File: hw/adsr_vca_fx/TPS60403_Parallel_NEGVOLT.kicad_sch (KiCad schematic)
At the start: 9 parts

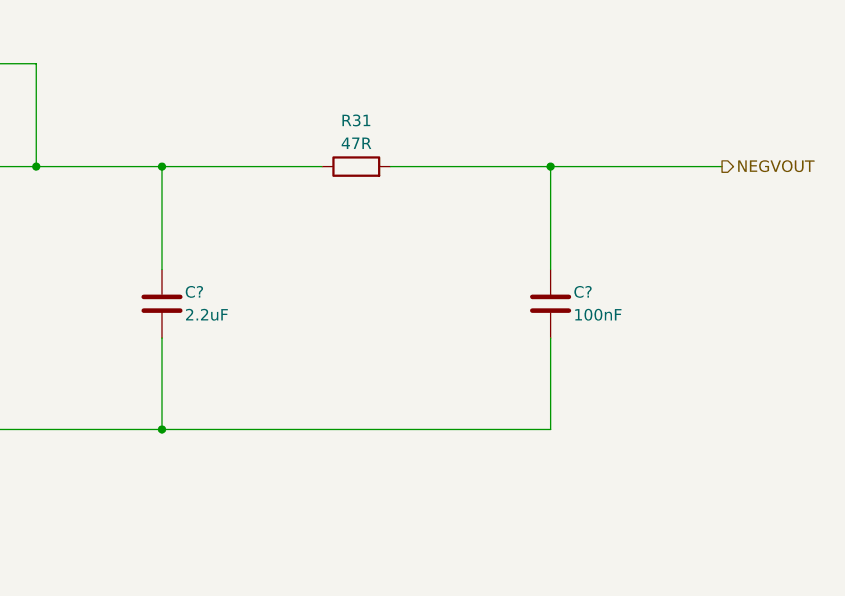
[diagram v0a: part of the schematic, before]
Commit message: renamed sheet
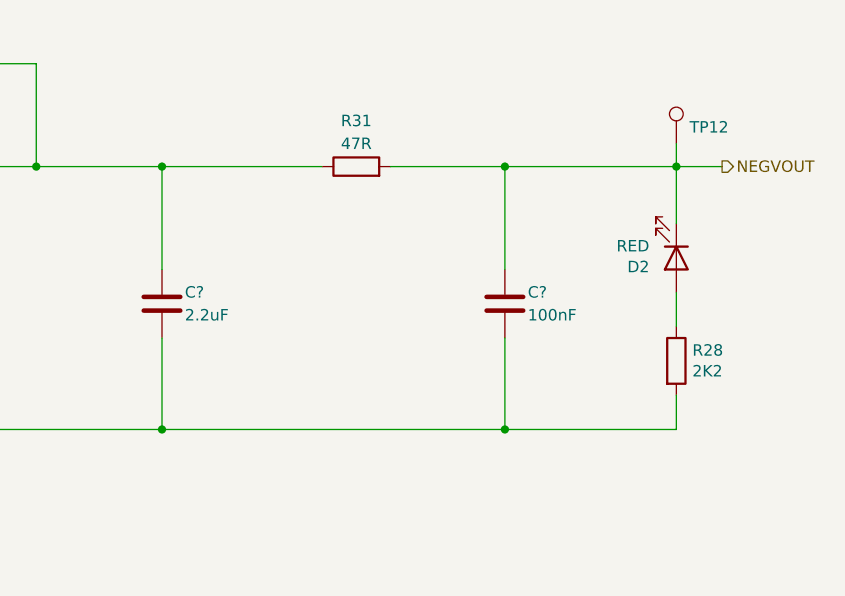
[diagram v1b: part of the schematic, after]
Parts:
- added D2: RED, LED_SMD:LED_0805_2012Metric_Pad1.15x1.40mm_HandSolder, symbol Device:LED
- added R28: 2K2, Resistor_SMD:R_0805_2012Metric_Pad1.20x1.40mm_HandSolder, symbol Device:R
- added TP12: TestPoint, TestPoint:TestPoint_Pad_D1.0mm, symbol Connector:TestPoint
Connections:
- net GND: now also R28.2
- net NEGVOUT: now also D2.1 (K), TP12.1
- new net: D2.2 (A), R28.1
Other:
- moved on the sheet: C?
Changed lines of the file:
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@@
 (kicad_sch (version 20230121) (generator eeschema)
   (paper "A4")
-  (junction (at 240.03 69.85) (diameter 0) (color 0 0 0 0)
-  )
   (junction (at 196.85 99.06) (diameter 0) (color 0 0 0 0)
   )
@@
   (junction (at 66.04 55.88) (diameter 0) (color 0 0 0 0)
   )
+  (junction (at 234.95 99.06) (diameter 0) (color 0 0 0 0)
+  )
   (junction (at 182.88 69.85) (diameter 0) (color 0 0 0 0)
   )
   (junction (at 176.53 99.06) (diameter 0) (color 0 0 0 0)
   )
+  (junction (at 254 69.85) (diameter 0) (color 0 0 0 0)
+  )
+  (junction (at 234.95 69.85) (diameter 0) (color 0 0 0 0)
+  )
   (wire (pts (xy 196.85 69.85) (xy 196.85 81.28))
     (stroke (width 0) (type default))
@@
     (stroke (width 0) (type default))
   )
+  (wire (pts (xy 254 69.85) (xy 254 67.31))
+    (stroke (width 0) (type default))
+  )
   (wire (pts (xy 87.63 72.39) (xy 93.98 72.39))
     (stroke (width 0) (type default))
   )
-  (wire (pts (xy 240.03 69.85) (xy 240.03 81.28))
+  (wire (pts (xy 234.95 69.85) (xy 234.95 81.28))
     (stroke (width 0) (type default))
   )
@@
     (stroke (width 0) (type default))
   )
+  (wire (pts (xy 234.95 99.06) (xy 254 99.06))
+    (stroke (width 0) (type default))
+  )
+  (wire (pts (xy 254 87.63) (xy 254 83.82))
+    (stroke (width 0) (type default))
+  )
   (wire (pts (xy 123.19 82.55) (xy 123.19 99.06))
     (stroke (width 0) (type default))
@@
     (stroke (width 0) (type default))
   )
-  (wire (pts (xy 240.03 99.06) (xy 196.85 99.06))
+  (wire (pts (xy 254 69.85) (xy 254 76.2))
     (stroke (width 0) (type default))
   )
@@
     (stroke (width 0) (type default))
   )
-  (wire (pts (xy 240.03 88.9) (xy 240.03 99.06))
+  (wire (pts (xy 234.95 88.9) (xy 234.95 99.06))
     (stroke (width 0) (type default))
   )
@@
     (stroke (width 0) (type default))
   )
-  (wire (pts (xy 222.25 69.85) (xy 240.03 69.85))
-    (stroke (width 0) (type default))
-  )
-  (wire (pts (xy 240.03 69.85) (xy 259.08 69.85))
+  (wire (pts (xy 222.25 69.85) (xy 234.95 69.85))
+    (stroke (width 0) (type default))
+  )
+  (wire (pts (xy 234.95 99.06) (xy 196.85 99.06))
+    (stroke (width 0) (type default))
+  )
+  (wire (pts (xy 254 69.85) (xy 259.08 69.85))
+    (stroke (width 0) (type default))
+  )
+  (wire (pts (xy 254 95.25) (xy 254 99.06))
+    (stroke (width 0) (type default))
+  )
+  (wire (pts (xy 234.95 69.85) (xy 254 69.85))
     (stroke (width 0) (type default))
   )
@@
     )
   )
+  (symbol (lib_id "Device:R") (at 254 91.44 0) (unit 1)
+    (in_bom yes) (on_board yes) (dnp no)
+    (property "Reference" "R28" (at 255.778 90.2716 0)
+      (effects (font (size 1.27 1.27)) (justify left))
+    )
+    (property "Value" "2K2" (at 255.778 92.583 0)
+      (effects (font (size 1.27 1.27)) (justify left))
+    )
+    (property "Footprint" "Resistor_SMD:R_0805_2012Metric_Pad1.20x1.40mm_HandSolder" (at 252.222 91.44 90)
+      (effects (font (size 1.27 1.27)) hide)
+    )
+    (property "Datasheet" "~" (at 254 91.44 0)
+      (effects (font (size 1.27 1.27)) hide)
+    )
+    (property "LcscNo" "~" (at 254 91.44 0)
+      (effects (font (size 1.27 1.27)) hide)
+    )
+    (property "Type" "~" (at 254 91.44 0)
+      (effects (font (size 1.27 1.27)) hide)
+    )
+    (pin "1")
+    (pin "2")
+    (instances
+      (project "adsr_vca_fx"
+        (path "/2c7cc946-dcca-4ffb-b6a0-bf0c9ddb491b/d2509004-b5c4-4b3c-af62-d7c90bd19790/2b12c81b-590f-42b3-a93e-f9019ce43b66"
+          (reference "R28") (unit 1)
+        )
+        (path "/2c7cc946-dcca-4ffb-b6a0-bf0c9ddb491b/d2509004-b5c4-4b3c-af62-d7c90bd19790/8209921e-d4bf-4a54-a276-7037229ad038"
+          (reference "R20") (unit 1)
+        )
+      )
+    )
+  )
   (symbol (lib_id "TPS6040x:TPS60400") (at 104.14 76.2 0) (unit 1)
     (in_bom yes) (on_board yes) (dnp no) (fields_autoplaced)
@@
     )
   )
-  (symbol (lib_id "Device:C") (at 240.03 85.09 0) (unit 1)
+  (symbol (lib_id "Device:C") (at 234.95 85.09 0) (unit 1)
     (in_bom yes) (on_board yes) (dnp no)
-    (property "Reference" "C?" (at 242.57 83.82 0)
-      (effects (font (size 1.27 1.27)) (justify left))
-    )
-    (property "Value" "100nF" (at 242.57 86.36 0)
-      (effects (font (size 1.27 1.27)) (justify left))
-    )
-    (property "Footprint" "Capacitor_SMD:C_0805_2012Metric_Pad1.18x1.45mm_HandSolder" (at 240.9952 88.9 0)
-      (effects (font (size 1.27 1.27)) hide)
-    )
-    (property "Datasheet" "~" (at 240.03 85.09 0)
+    (property "Reference" "C?" (at 237.49 83.82 0)
+      (effects (font (size 1.27 1.27)) (justify left))
+    )
+    (property "Value" "100nF" (at 237.49 86.36 0)
+      (effects (font (size 1.27 1.27)) (justify left))
+    )
+    (property "Footprint" "Capacitor_SMD:C_0805_2012Metric_Pad1.18x1.45mm_HandSolder" (at 235.9152 88.9 0)
+      (effects (font (size 1.27 1.27)) hide)
+    )
+    (property "Datasheet" "~" (at 234.95 85.09 0)
       (effects (font (size 1.27 1.27)) hide)
     )
@@
     )
   )
+  (symbol (lib_id "Device:LED") (at 254 80.01 270) (unit 1)
+    (in_bom yes) (on_board yes) (dnp no)
+    (property "Reference" "D2" (at 251.0028 81.0006 90)
+      (effects (font (size 1.27 1.27)) (justify right))
+    )
+    (property "Value" "RED" (at 251.0028 78.6892 90)
+      (effects (font (size 1.27 1.27)) (justify right))
+    )
+    (property "Footprint" "LED_SMD:LED_0805_2012Metric_Pad1.15x1.40mm_HandSolder" (at 254 80.01 0)
+      (effects (font (size 1.27 1.27)) hide)
+    )
+    (property "Datasheet" "~" (at 254 80.01 0)
+      (effects (font (size 1.27 1.27)) hide)
+    )
+    (property "LcscNo" "C2293" (at 254 80.01 0)
+      (effects (font (size 1.27 1.27)) hide)
+    )
+    (property "Type" "~" (at 254 80.01 0)
+      (effects (font (size 1.27 1.27)) hide)
+    )
+    (pin "1")
+    (pin "2")
+    (instances
+      (project "adsr_vca_fx"
+        (path "/2c7cc946-dcca-4ffb-b6a0-bf0c9ddb491b/d2509004-b5c4-4b3c-af62-d7c90bd19790/2b12c81b-590f-42b3-a93e-f9019ce43b66"
+          (reference "D2") (unit 1)
+        )
+        (path "/2c7cc946-dcca-4ffb-b6a0-bf0c9ddb491b/d2509004-b5c4-4b3c-af62-d7c90bd19790/8209921e-d4bf-4a54-a276-7037229ad038"
+          (reference "D5") (unit 1)
+        )
+      )
+    )
+  )
   (symbol (lib_id "Device:C") (at 66.04 83.82 0) (unit 1)
     (in_bom yes) (on_board yes) (dnp no) (fields_autoplaced)
@@
         )
       )
+    )
+  )
+  (symbol (lib_id "Connector:TestPoint") (at 254 67.31 0) (unit 1)
+    (in_bom yes) (on_board yes) (dnp no)
+    (property "Reference" "TP12" (at 255.4732 65.4812 0)
+      (effects (font (size 1.27 1.27)) (justify left))
+    )
+    (property "Value" "TestPoint" (at 255.4732 66.6242 0)
+      (effects (font (size 1.27 1.27)) (justify left) hide)
+    )
+    (property "Footprint" "TestPoint:TestPoint_Pad_D1.0mm" (at 259.08 67.31 0)
+      (effects (font (size 1.27 1.27)) hide)
+    )
+    (property "Datasheet" "~" (at 259.08 67.31 0)
+      (effects (font (size 1.27 1.27)) hide)
+    )
+    (property "LcscNo" "~" (at 254 67.31 0)
+      (effects (font (size 1.27 1.27)) hide)
+    )
+    (property "Type" "~" (at 254 67.31 0)
+      (effects (font (size 1.27 1.27)) hide)
+    )
+    (pin "1")
+    (instances
+      (project "adsr_vca_fx"
+        (path "/2c7cc946-dcca-4ffb-b6a0-bf0c9ddb491b/d2509004-b5c4-4b3c-af62-d7c90bd19790/2b12c81b-590f-42b3-a93e-f9019ce43b66"
+          (reference "TP12") (unit 1)
+        )
+        (path "/2c7cc946-dcca-4ffb-b6a0-bf0c9ddb491b/d2509004-b5c4-4b3c-af62-d7c90bd19790/8209921e-d4bf-4a54-a276-7037229ad038"
+          (reference "TP3") (unit 1)
+        )
+      )

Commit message: first draft layout
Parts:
- renumbered R31 to R27
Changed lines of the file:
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@@
   (symbol (lib_id "Device:R") (at 218.44 69.85 90) (unit 1)
     (in_bom yes) (on_board yes) (dnp no) (fields_autoplaced)
-    (property "Reference" "R31" (at 218.44 64.77 90)
+    (property "Reference" "R27" (at 218.44 64.77 90)
       (effects (font (size 1.27 1.27)))
     )
@@
       (project "adsr_vca_fx"
         (path "/2c7cc946-dcca-4ffb-b6a0-bf0c9ddb491b/d2509004-b5c4-4b3c-af62-d7c90bd19790/8209921e-d4bf-4a54-a276-7037229ad038"
-          (reference "R31") (unit 1)
+          (reference "R27") (unit 1)
         )
       )
@@
   (symbol (lib_id "power:GND") (at 123.19 109.22 0) (unit 1)
     (in_bom yes) (on_board yes) (dnp no) (fields_autoplaced)
-    (property "Reference" "#PWR071" (at 123.19 115.57 0)
+    (property "Reference" "#PWR069" (at 123.19 115.57 0)
       (effects (font (size 1.27 1.27)) hide)
     )
@@
       (project "adsr_vca_fx"
         (path "/2c7cc946-dcca-4ffb-b6a0-bf0c9ddb491b/d2509004-b5c4-4b3c-af62-d7c90bd19790/8209921e-d4bf-4a54-a276-7037229ad038"
-          (reference "#PWR071") (unit 1)
+          (reference "#PWR069") (unit 1)
         )
       )
@@
         )
         (path "/2c7cc946-dcca-4ffb-b6a0-bf0c9ddb491b/d2509004-b5c4-4b3c-af62-d7c90bd19790/8209921e-d4bf-4a54-a276-7037229ad038"
-          (reference "U12") (unit 1)
+          (reference "U9") (unit 1)
         )
       )
@@
         )
         (path "/2c7cc946-dcca-4ffb-b6a0-bf0c9ddb491b/d2509004-b5c4-4b3c-af62-d7c90bd19790/8209921e-d4bf-4a54-a276-7037229ad038"
-          (reference "R20") (unit 1)
+          (reference "R28") (unit 1)
         )
       )
@@
         )
         (path "/2c7cc946-dcca-4ffb-b6a0-bf0c9ddb491b/d2509004-b5c4-4b3c-af62-d7c90bd19790/8209921e-d4bf-4a54-a276-7037229ad038"
-          (reference "U11") (unit 1)
+          (reference "U8") (unit 1)
         )
       )
@@
         )
         (path "/2c7cc946-dcca-4ffb-b6a0-bf0c9ddb491b/d2509004-b5c4-4b3c-af62-d7c90bd19790/8209921e-d4bf-4a54-a276-7037229ad038"
-          (reference "C33") (unit 1)
+          (reference "C27") (unit 1)
         )
       )
@@
         )
         (path "/2c7cc946-dcca-4ffb-b6a0-bf0c9ddb491b/d2509004-b5c4-4b3c-af62-d7c90bd19790/8209921e-d4bf-4a54-a276-7037229ad038"
-          (reference "C30") (unit 1)
+          (reference "C24") (unit 1)
         )
       )
@@
         )
         (path "/2c7cc946-dcca-4ffb-b6a0-bf0c9ddb491b/d2509004-b5c4-4b3c-af62-d7c90bd19790/8209921e-d4bf-4a54-a276-7037229ad038"
-          (reference "C29") (unit 1)
+          (reference "C23") (unit 1)
         )
       )
@@
         )
         (path "/2c7cc946-dcca-4ffb-b6a0-bf0c9ddb491b/d2509004-b5c4-4b3c-af62-d7c90bd19790/8209921e-d4bf-4a54-a276-7037229ad038"
-          (reference "TP3") (unit 1)
+          (reference "TP11") (unit 1)
         )
       )
@@
         )
         (path "/2c7cc946-dcca-4ffb-b6a0-bf0c9ddb491b/d2509004-b5c4-4b3c-af62-d7c90bd19790/8209921e-d4bf-4a54-a276-7037229ad038"
-          (reference "C32") (unit 1)
+          (reference "C26") (unit 1)
         )
       )
@@
         )
         (path "/2c7cc946-dcca-4ffb-b6a0-bf0c9ddb491b/d2509004-b5c4-4b3c-af62-d7c90bd19790/8209921e-d4bf-4a54-a276-7037229ad038"
-          (reference "C31") (unit 1)
-        )
-      )
+          (reference "C25") (unit 1)
+        )
+      )

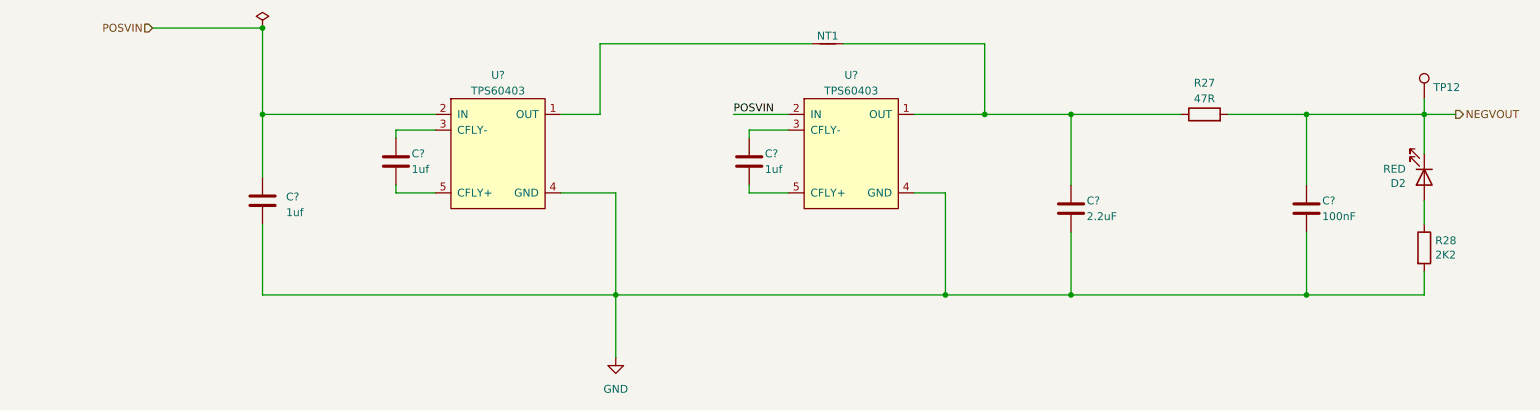
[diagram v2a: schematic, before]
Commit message: updated layout
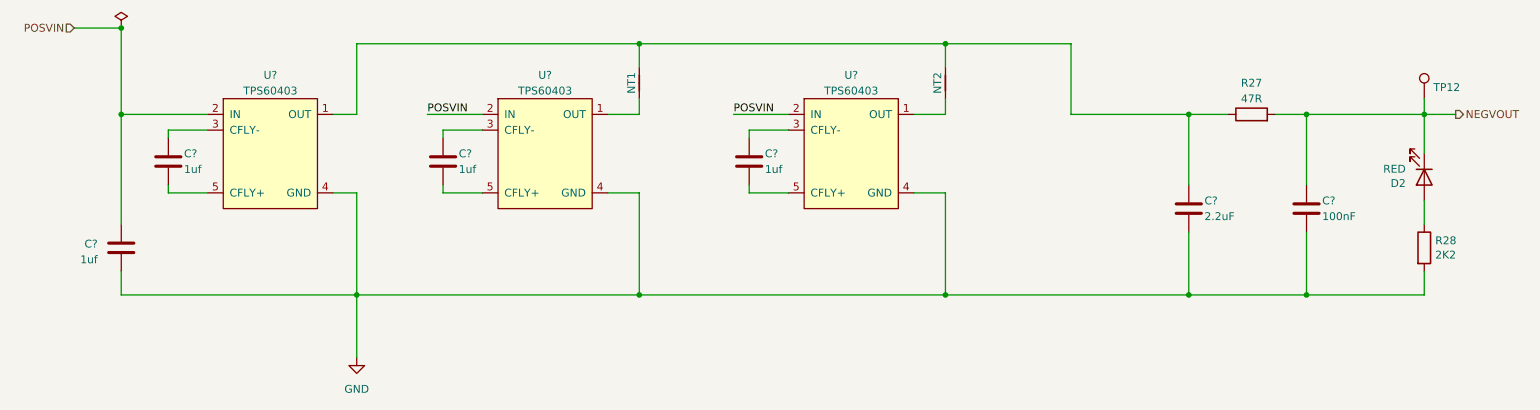
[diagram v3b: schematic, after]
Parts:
- added C?: 1uf, Capacitor_SMD:C_0805_2012Metric_Pad1.18x1.45mm_HandSolder, symbol Device:C
- added NT2: NetTie_2, NetTie:NetTie-2_SMD_Pad0.5mm, symbol Device:NetTie_2
- added U?: TPS60403, Package_TO_SOT_SMD:SOT-23-5_HandSoldering, symbol TPS6040x:TPS60400
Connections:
- net GND: now also U?.4 (GND)
- net POSVIN: now also U?.2 (IN)
- net at C?.1, NT1.2, R27.1: now also U?.1 (OUT), NT2.2; no longer U?.1 (OUT)
- net at NT1.1: now also U?.1 (OUT); no longer U?.1 (OUT)
- new net: NT2.1, U?.1 (OUT)
- new net: C?.1, U?.3 (CFLY-)
- new net: C?.2, U?.5 (CFLY+)
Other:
- moved on the sheet: C?, NT1, R27, U?

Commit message: completed layout
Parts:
- removed TP12: TestPoint, TestPoint:TestPoint_Pad_D1.0mm, symbol Connector:TestPoint
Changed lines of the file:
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@@
-    (stroke (width 0) (type default))
-  )
-  (wire (pts (xy 254 69.85) (xy 254 67.31))
     (stroke (width 0) (type default))
   )
@@
         )
       )
-    )
-  )
-  (symbol (lib_id "Connector:TestPoint") (at 254 67.31 0) (unit 1)
-    (in_bom yes) (on_board yes) (dnp no)
-    (property "Reference" "TP12" (at 255.4732 65.4812 0)
-      (effects (font (size 1.27 1.27)) (justify left))
-    )
-    (property "Value" "TestPoint" (at 255.4732 66.6242 0)
-      (effects (font (size 1.27 1.27)) (justify left) hide)
-    )
-    (property "Footprint" "TestPoint:TestPoint_Pad_D1.0mm" (at 259.08 67.31 0)
-      (effects (font (size 1.27 1.27)) hide)
-    )
-    (property "Datasheet" "~" (at 259.08 67.31 0)
-      (effects (font (size 1.27 1.27)) hide)
-    )
-    (property "LcscNo" "~" (at 254 67.31 0)
-      (effects (font (size 1.27 1.27)) hide)
-    )
-    (property "Type" "~" (at 254 67.31 0)
-      (effects (font (size 1.27 1.27)) hide)
-    )
-    (pin "1")
-    (instances
-      (project "adsr_vca_fx"
-        (path "/2c7cc946-dcca-4ffb-b6a0-bf0c9ddb491b/d2509004-b5c4-4b3c-af62-d7c90bd19790/2b12c81b-590f-42b3-a93e-f9019ce43b66"
-          (reference "TP12") (unit 1)
-        )
-        (path "/2c7cc946-dcca-4ffb-b6a0-bf0c9ddb491b/d2509004-b5c4-4b3c-af62-d7c90bd19790/8209921e-d4bf-4a54-a276-7037229ad038"
-          (reference "TP11") (unit 1)
-        )
-      )
